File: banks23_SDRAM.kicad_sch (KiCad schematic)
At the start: 6 parts, among them U1 NX1H35 PBGA625, U3 AS4C8M32S-6TIN

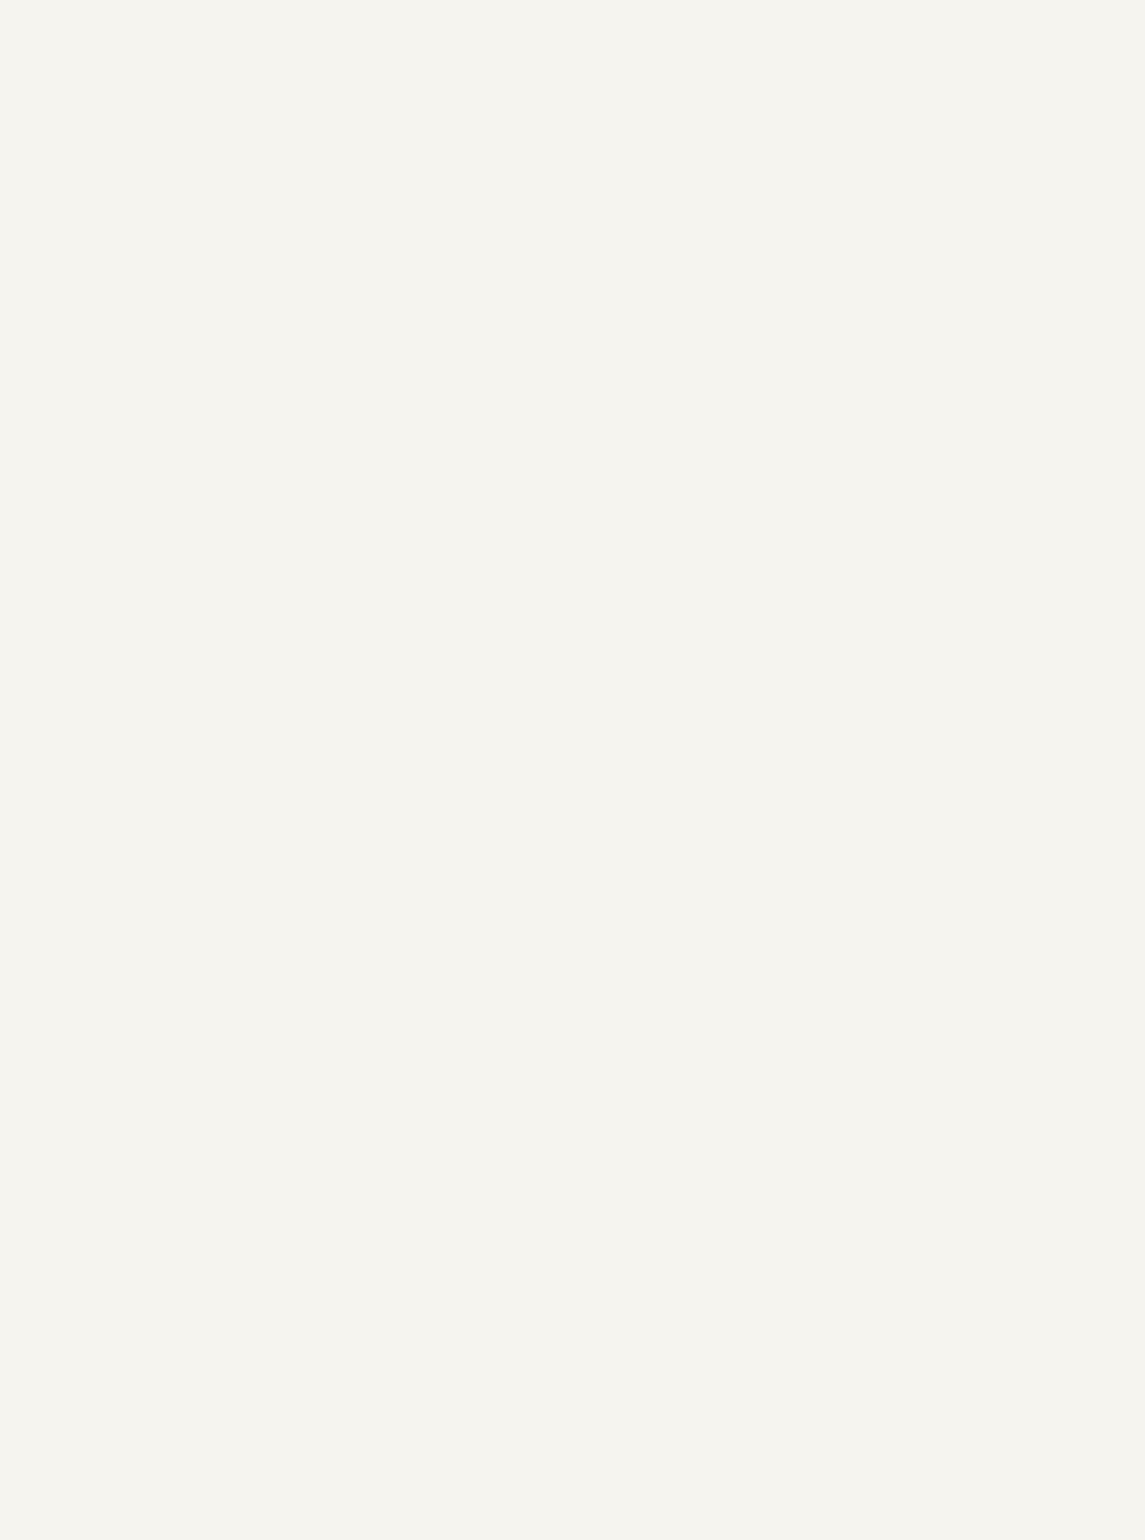
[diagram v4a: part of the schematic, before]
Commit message: added extra decoupling capacitors
extra decoupling on 2V5IO and Service rails
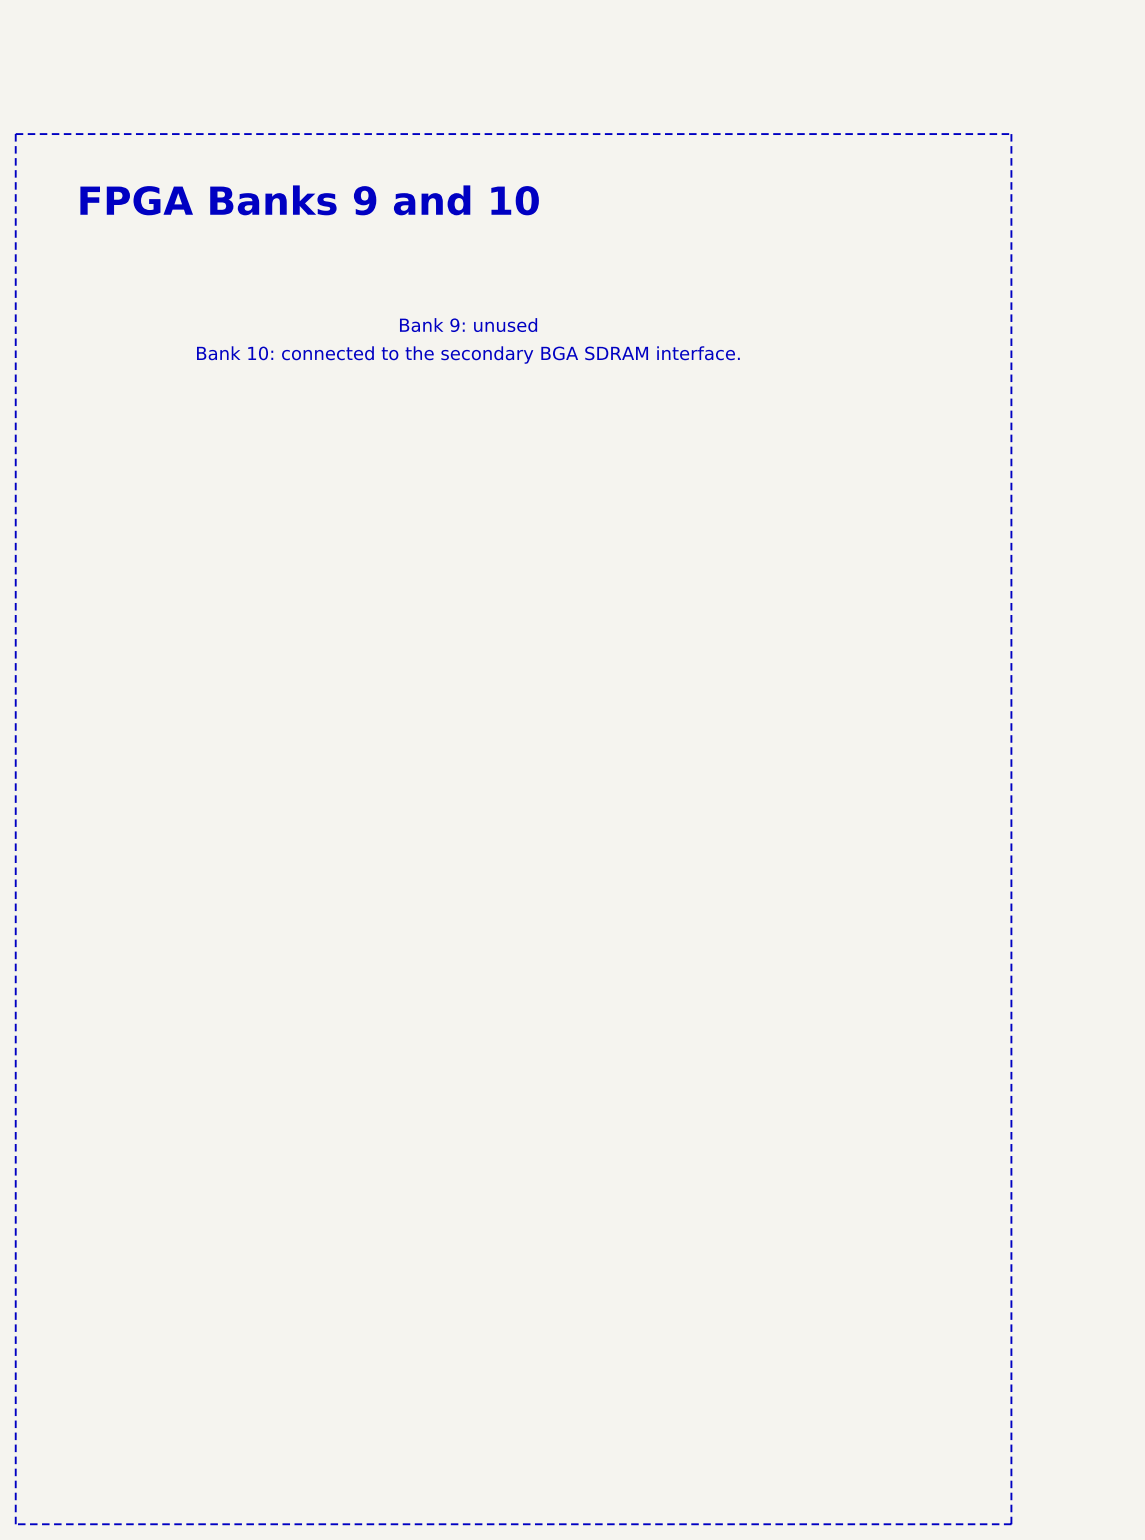
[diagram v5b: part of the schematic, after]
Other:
- note added: "Bank 10: connected to the secondary BGA SDRAM interface."
- note added: "Bank 9: unused"
- note added: "FPGA Banks 9 and 10"
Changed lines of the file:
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@@
 	(generator_version "9.0")
 	(paper "A3")
+	(rectangle
+		(start -144.78 45.72)
+		(end -10.16 233.68)
+		(stroke
+			(width 0.254)
+			(type dash)
+		)
+		(fill
+			(type none)
+		)
+	)
+	(text "Bank 10: connected to the secondary BGA SDRAM interface."
+		(exclude_from_sim no)
+		(at -83.566 75.692 0)
+		(effects
+			(font
+				(size 1.778 1.778)
+			)
+		)
+	)
+	(text "FPGA Banks 9 and 10"
+		(exclude_from_sim no)
+		(at -105.156 55.118 0)
+		(effects
+			(font
+				(size 3.81 3.81)
+				(thickness 0.762)
+				(bold yes)
+			)
+		)
+	)
+	(text "Bank 9: unused"
+		(exclude_from_sim no)
+		(at -83.566 71.882 0)
+		(effects
+			(font
+				(size 1.778 1.778)
+				(color 72 0 0 1)
+			)
+		)
+	)
 	(junction
 		(at 243.84 144.78)
